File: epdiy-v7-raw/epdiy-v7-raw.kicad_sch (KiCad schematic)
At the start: 104 parts, among them CN1 WP27D-S050VA3-R15000, J1 USB_C_Receptacle_USB2.0, J2 EXTENSION_HEADER, J4 XF2M-3315-1A, J5 CONN_BAT, J7 ESP_HDR, Q1 AO3401A, SW1 TC-0522C-1.7-160G, SW2 TC-0522C-1.7-160G, U1 RT9080-33GJ5, U10 ED060XC5, U11 TP4056, U3 TPS651851RSLR, U4 USBLC6-2P6, U8 ESP32-S3-WROOM-1, Y1 RV-3032-C7

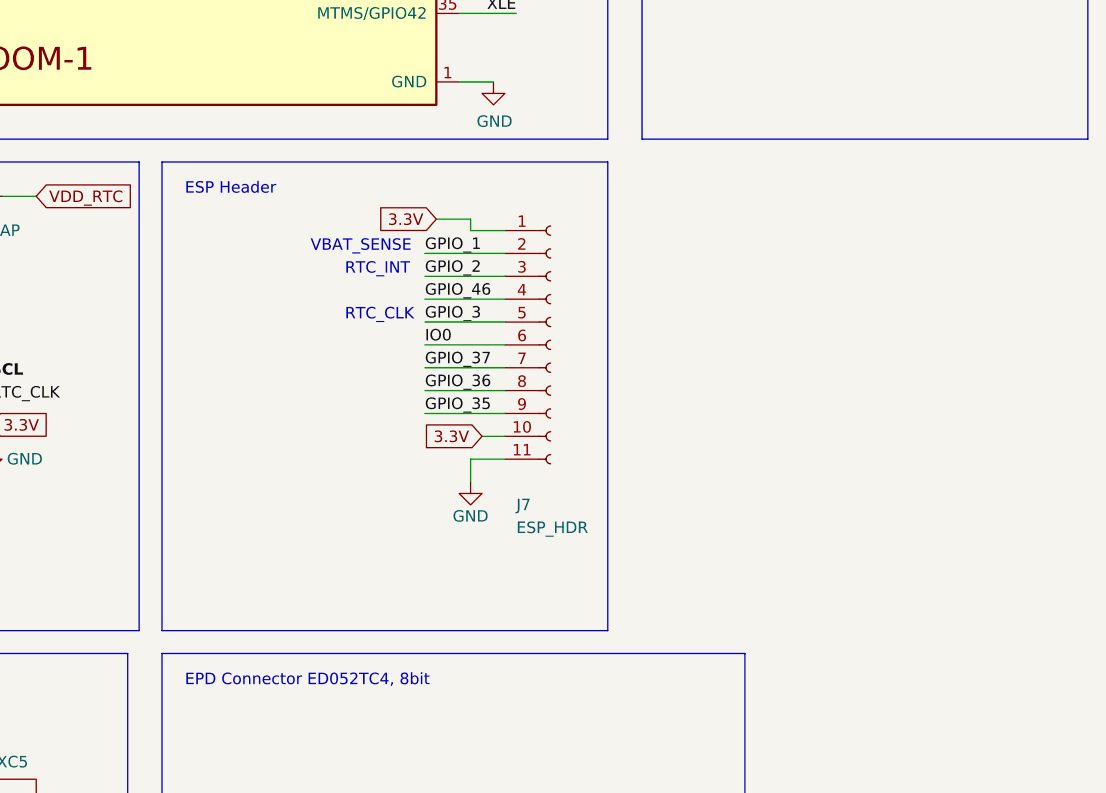
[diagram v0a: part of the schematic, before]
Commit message: Add signals test header
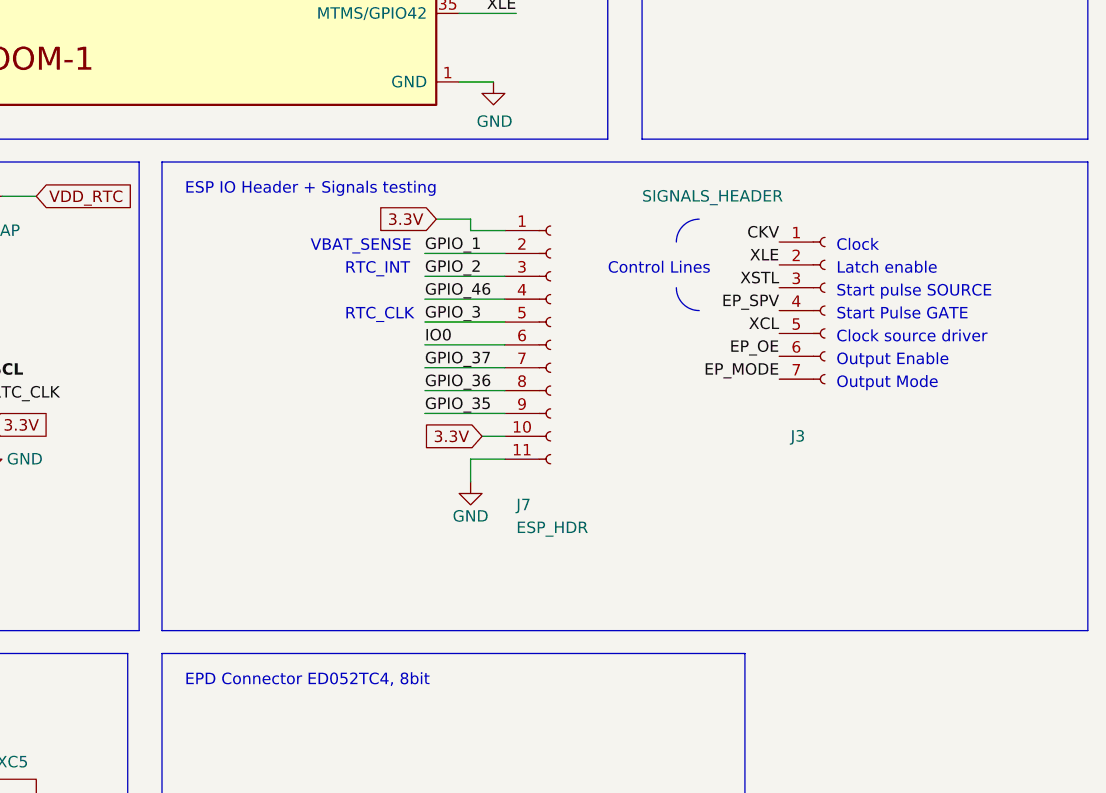
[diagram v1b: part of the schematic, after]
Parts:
- added J3: SIGNALS_HEADER, Connector_PinHeader_2.54mm:PinHeader_1x07_P2.54mm_Vertical, symbol Connector:Conn_01x07_Socket
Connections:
- net CKV: now also J3.1 (Pin_1)
- net EP_MODE: now also J3.7 (Pin_7)
- net EP_OE: now also J3.6 (Pin_6)
- net EP_SPV: now also J3.4 (Pin_4)
- net XCL: now also J3.5 (Pin_5)
- net XLE: now also J3.2 (Pin_2)
- net XSTL: now also J3.3 (Pin_3)
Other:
- note added: "Clock"
- note added: "Clock source driver"
- note added: "Control Lines"
- note added: "ESP IO Header + Signals testing"
- note added: "Latch enable"
- note added: "Output Enable"
- note added: "Output Mode"
- note added: "Start Pulse GATE"
- note added: "Start pulse SOURCE"
- note removed: "ESP Header"
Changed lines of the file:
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@@
     (stroke (width 0) (type default))
   )
-  (polyline (pts (xy 384.81 162.56) (xy 335.28 162.56))
+  (polyline (pts (xy 438.15 162.56) (xy 335.28 162.56))
     (stroke (width 0) (type default))
   )
@@
     (stroke (width 0) (type default))
   )
-  (polyline (pts (xy 335.28 110.49) (xy 384.81 110.49))
+  (polyline (pts (xy 335.28 110.49) (xy 438.15 110.49))
     (stroke (width 0) (type default))
   )
@@
     (stroke (width 0) (type default))
   )
-  (polyline (pts (xy 384.81 110.49) (xy 384.81 162.56))
+  (polyline (pts (xy 438.15 110.49) (xy 438.15 162.56))
     (stroke (width 0) (type default))
   )
@@
     (fill (type none))
   )
+  (arc (start 394.97 127) (mid 393.1739 126.2561) (end 392.43 124.46)
+    (stroke (width 0) (type default))
+    (fill (type none))
+  )
   (rectangle (start 284.48 165.1) (end 331.47 275.59)
     (stroke (width 0) (type default))
     (fill (type none))
   )
+  (arc (start 392.43 119.38) (mid 393.1739 117.5839) (end 394.97 116.84)
+    (stroke (width 0) (type default))
+    (fill (type none))
+  )
   (rectangle (start 129.54 33.02) (end 205.74 77.47)
     (stroke (width 0) (type default))
     (fill (type none))
   )
+  (text "Start pulse SOURCE" (at 410.21 125.73 0)
+    (effects (font (size 1.27 1.27)) (justify left bottom))
+  )
   (text "Battery Voltage Sense" (at 209.55 114.3 0)
     (effects (font (size 1.27 1.27)) (justify left bottom))
@@
     (effects (font (size 1.27 1.27)) (justify left bottom))
   )
-  (text "ESP Header" (at 337.82 114.3 0)
+  (text "ESP IO Header + Signals testing" (at 337.82 114.3 0)
     (effects (font (size 1.27 1.27)) (justify left bottom))
   )
@@
     (effects (font (size 1.27 1.27)) (justify left bottom))
   )
+  (text "Clock" (at 410.21 120.65 0)
+    (effects (font (size 1.27 1.27)) (justify left bottom))
+  )
   (text "EPD Connector ED052TC4, 8bit" (at 337.82 168.91 0)
     (effects (font (size 1.27 1.27)) (justify left bottom))
@@
     (effects (font (size 1.27 1.27)) (justify left bottom))
   )
+  (text "Clock source driver" (at 410.21 130.81 0)
+    (effects (font (size 1.27 1.27)) (justify left bottom))
+  )
   (text "▴ superCAP needs ▴\nto be hand-soldered" (at 265.43 124.46 0)
     (effects (font (size 1 1) (color 194 0 0 1)) (justify left bottom))
@@
     (effects (font (size 1.27 1.27)) (justify left bottom))
   )
+  (text "Output Enable" (at 410.21 133.35 0)
+    (effects (font (size 1.27 1.27)) (justify left bottom))
+  )
   (text "RESET" (at 154.94 74.93 0)
     (effects (font (size 1.27 1.27)) (justify left bottom))
@@
     (effects (font (size 1.27 1.27)) (justify left bottom))
   )
+  (text "Latch enable" (at 410.21 123.19 0)
+    (effects (font (size 1.27 1.27)) (justify left bottom))
+  )
   (text "VBAT_SENSE" (at 351.79 120.65 0)
     (effects (font (size 1.27 1.27) (color 194 0 194 1)) (justify left bottom))
   )
+  (text "Start Pulse GATE" (at 410.21 128.27 0)
+    (effects (font (size 1.27 1.27)) (justify left bottom))
+  )
   (text "EPD Connector 34pin, 8bit" (at 288.925 168.91 0)
     (effects (font (size 1.27 1.27)) (justify left bottom))
   )
+  (text "Output Mode" (at 410.21 135.89 0)
+    (effects (font (size 1.27 1.27)) (justify left bottom))
+  )
   (text "BOOT" (at 177.8 74.93 0)
     (effects (font (size 1.27 1.27)) (justify left bottom))
@@
     (effects (font (size 1.27 1.27)) (justify left bottom))
   )
+  (text "Control Lines" (at 384.81 123.19 0)
+    (effects (font (size 1.27 1.27)) (justify left bottom))
+  )
   (label "XLE" (at 374.65 93.98 180) (fields_autoplaced)
     (effects (font (size 1.27 1.27)) (justify right bottom))
@@
     (effects (font (size 1.27 1.27)) (justify left bottom))
   )
+  (label "CKV" (at 403.86 119.38 180) (fields_autoplaced)
+    (effects (font (size 1.27 1.27)) (justify right bottom))
+  )
   (label "LEH" (at 238.76 199.39 0) (fields_autoplaced)
     (effects (font (size 1.27 1.27)) (justify left bottom))
@@
     (effects (font (size 1.27 1.27)) (justify right bottom))
   )
+  (label "EP_MODE" (at 403.86 134.62 180) (fields_autoplaced)
+    (effects (font (size 1.27 1.27)) (justify right bottom))
+  )
   (label "VNEG_IN" (at 82.55 233.68 0) (fields_autoplaced)
     (effects (font (size 1.27 1.27)) (justify left bottom))
@@
     (effects (font (size 1.27 1.27)) (justify left bottom))
   )
+  (label "XLE" (at 403.86 121.92 180) (fields_autoplaced)
+    (effects (font (size 1.27 1.27)) (justify right bottom))
+  )
+  (label "XCL" (at 403.86 129.54 180) (fields_autoplaced)
+    (effects (font (size 1.27 1.27)) (justify right bottom))
+  )
   (label "D1" (at 369.57 236.22 0) (fields_autoplaced)
     (effects (font (size 1.27 1.27)) (justify left bottom))
@@
     (effects (font (size 1.27 1.27)) (justify right bottom))
   )
+  (label "XSTL" (at 403.86 124.46 180) (fields_autoplaced)
+    (effects (font (size 1.27 1.27)) (justify right bottom))
+  )
   (label "XLE" (at 300.99 204.47 0) (fields_autoplaced)
     (effects (font (size 1.27 1.27)) (justify left bottom))
@@
     (effects (font (size 1.27 1.27)) (justify left bottom))
   )
+  (label "EP_SPV" (at 403.86 127 180) (fields_autoplaced)
+    (effects (font (size 1.27 1.27)) (justify right bottom))
+  )
   (label "EP_SPV" (at 369.57 238.76 0) (fields_autoplaced)
     (effects (font (size 1.27 1.27)) (justify left bottom))
@@
     (effects (font (size 1.27 1.27)) (justify left bottom))
   )
+  (label "EP_OE" (at 403.86 132.08 180) (fields_autoplaced)
+    (effects (font (size 1.27 1.27)) (justify right bottom))
+  )
   (label "TPS_VCOM_CTRL" (at 247.65 78.74 180) (fields_autoplaced)
     (effects (font (size 1.27 1.27)) (justify right bottom))
@@
         )
       )
+    )
+  )
+  (symbol (lib_id "Connector:Conn_01x07_Socket") (at 408.94 127 0) (unit 1)
+    (in_bom yes) (on_board yes) (dnp no)
+    (property "Reference" "J3" (at 405.13 140.97 0)
+      (effects (font (size 1.27 1.27)) (justify left))
+    )
+    (property "Value" "SIGNALS_HEADER" (at 388.62 114.3 0)
+      (effects (font (size 1.27 1.27)) (justify left))
+    )
+    (property "Footprint" "Connector_PinHeader_2.54mm:PinHeader_1x07_P2.54mm_Vertical" (at 408.94 127 0)
+      (effects (font (size 1.27 1.27)) hide)
+    )
+    (property "Datasheet" "~" (at 408.94 127 0)
+      (effects (font (size 1.27 1.27)) hide)
+    )
+    (pin "1")
+    (pin "2")
+    (pin "3")
+    (pin "4")
+    (pin "5")
+    (pin "6")
+    (pin "7")
+    (instances
+      (project "epdiy-v7-raw"
+        (path "/d463a158-2b18-43e0-b0c5-d5462331aab1"
+          (reference "J3") (unit 1)
+        )
+      )

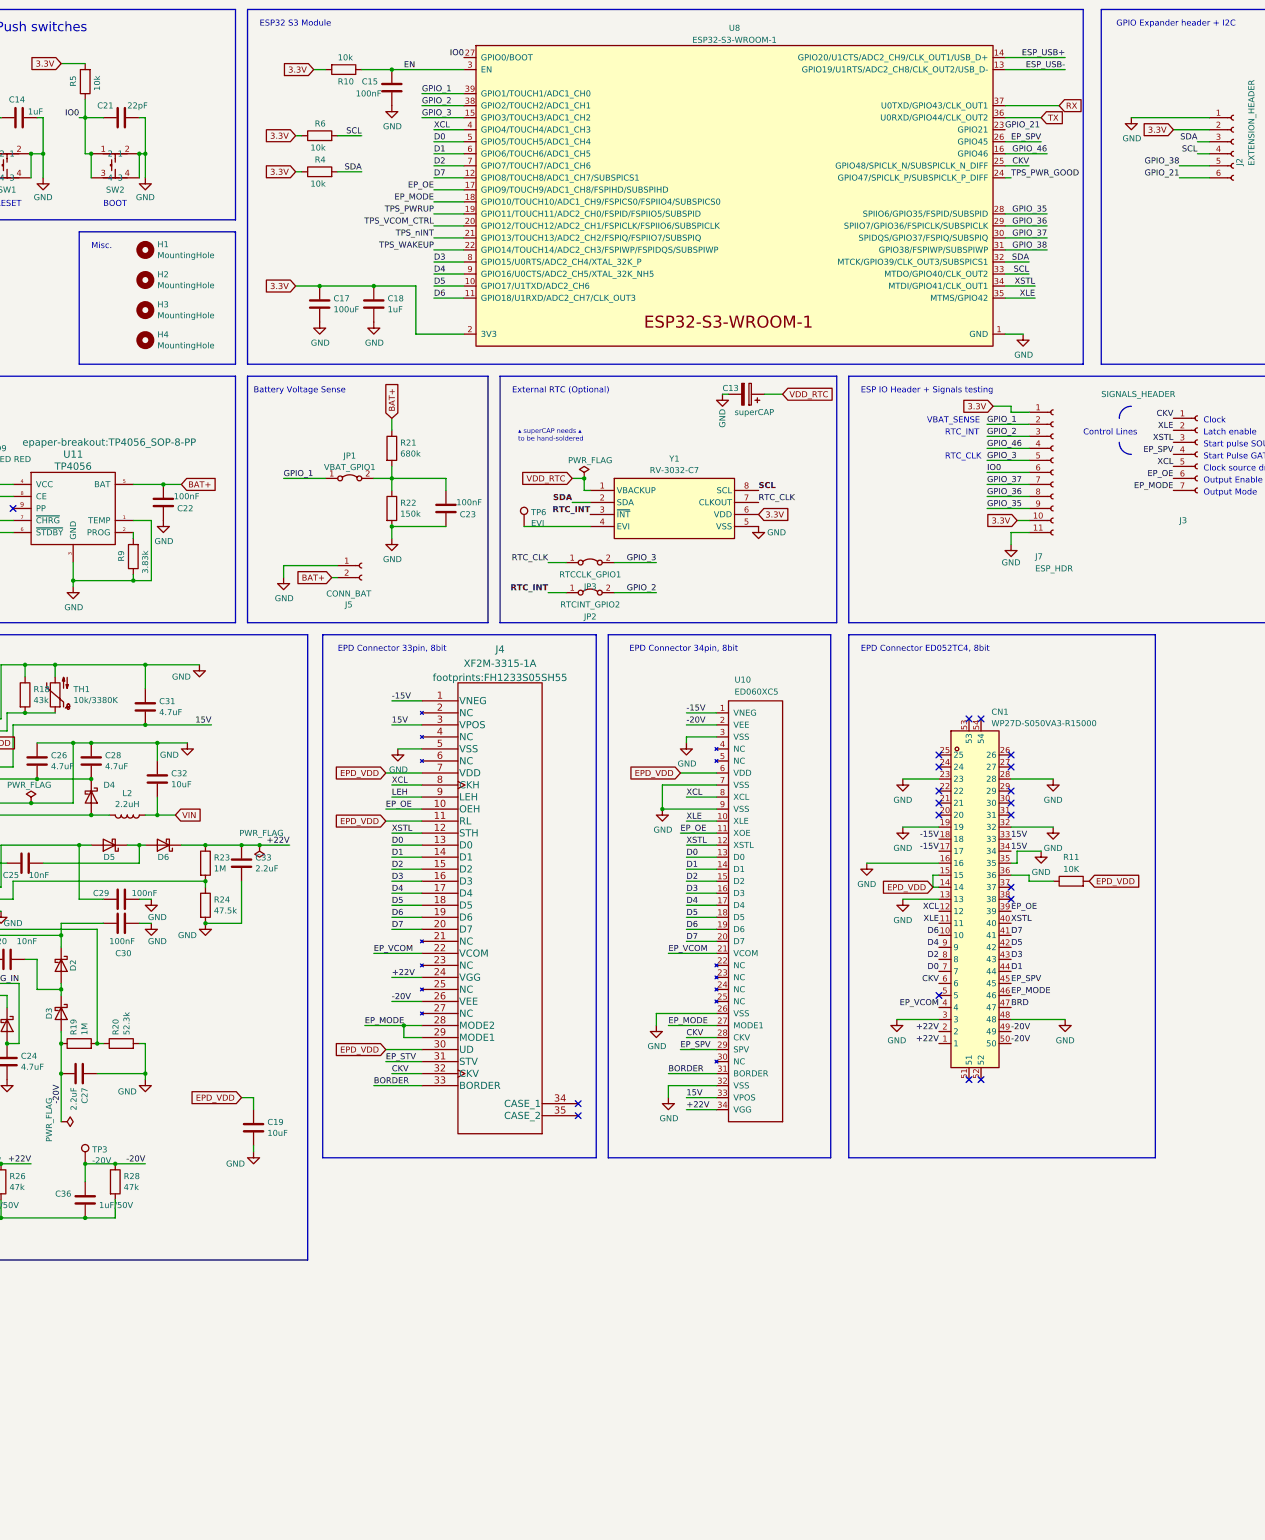
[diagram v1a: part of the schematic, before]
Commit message: Updated and NUT SMD corrected (KiCad 8)
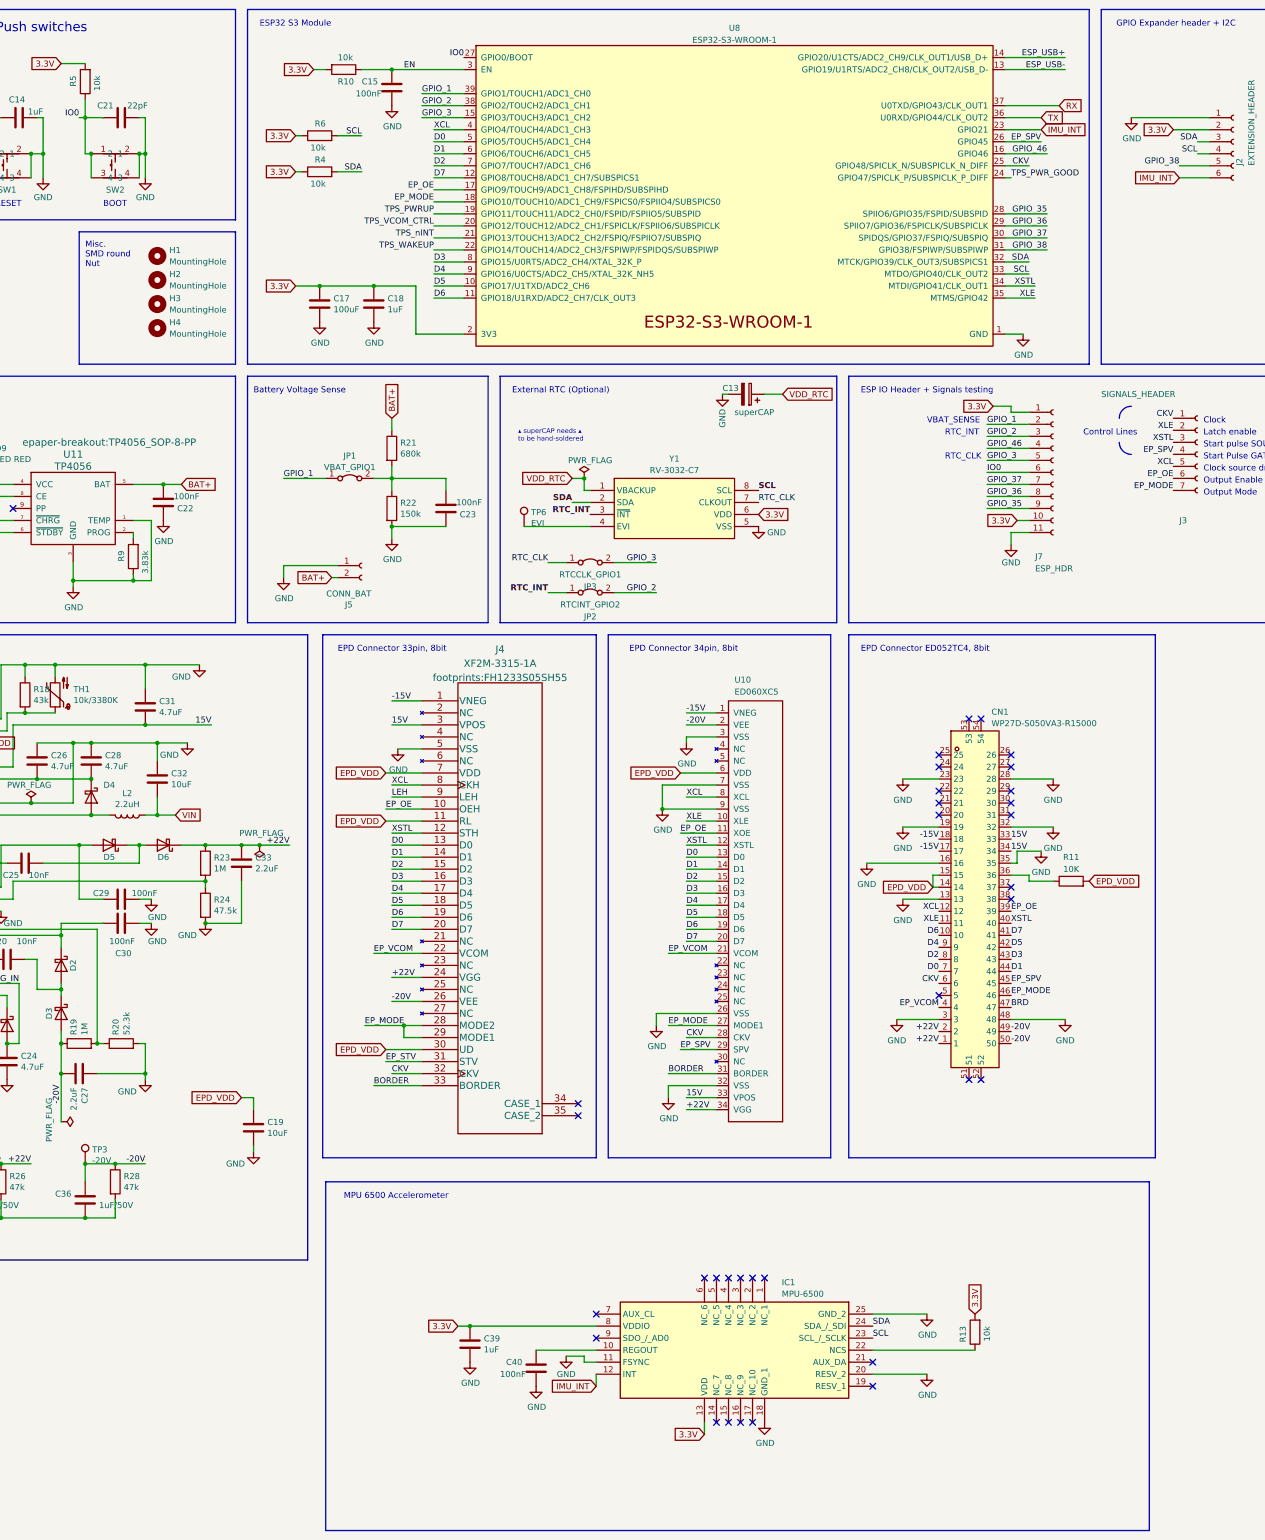
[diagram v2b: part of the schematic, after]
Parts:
- added C39: 1uF, Capacitor_SMD:C_0805_2012Metric, symbol Device:C
- added C40: 100nF, Capacitor_SMD:C_0805_2012Metric, symbol Device:C
- added IC1: MPU-6500, footprints:C50278_IMU_QFN-24_L3.0-W3.0-P0.40-BL-EP, symbol ACCEL:MPU-6500
- added R13: 10k, Resistor_SMD:R_0603_1608Metric, symbol Device:R
- H1, H2, H3, H4: footprint MountingHole:MountingHole_2.2mm_M2 -> footprints:C2916320_SMTSO2015CTJ; LCSC (none) -> C2916320; now in the parts list
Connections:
- net 3.3V: now also C39.2, IC1.13 (VDD), IC1.8 (VDDIO), R13.2
- net GND: now also C39.1, C40.2, IC1.11 (FSYNC), IC1.18 (GND_1), IC1.20 (RESV_2), IC1.25 (GND_2)
- net SCL: now also IC1.23 (SCL_/_SCLK)
- net SDA: now also IC1.24 (SDA_/_SDI)
- net GPIO_21 renamed IMU_INT
- net IMU_INT: now also IC1.12 (INT)
- new net: IC1.22 (NCS), R13.1
- new net: C40.1, IC1.10 (REGOUT)
- no-connect marks 27 -> 41
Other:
- note added: "MPU 6500 Accelerometer"
- note added: "Misc. SMD round Nut"
- note removed: "Misc."
